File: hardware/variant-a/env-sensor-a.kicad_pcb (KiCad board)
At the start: 4 copper layers, 30 x 34 mm, 64 parts, among them J1 USB-C 16P, J2 Molex PicoBlade 3P, Q1 2N7002, SW1 SW_PROV, U1 ESP32-C6-MINI-1-N4, U2 SHT45-AD1F, U3 TPS62840DLC, U4 BQ24074RGTR, U5 USBLC6-2SC6

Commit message: build(sch): regenerate connector mounting-ground connectivity
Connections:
- J2 pad MP: unconnected-(J2-MountPin-PadMP) -> GND
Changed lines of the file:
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@@
 	(net 36 "unconnected-(J1-SBU1-PadA8)")
 	(net 37 "unconnected-(J1-SBU2-PadB8)")
-	(net 38 "unconnected-(J2-MountPin-PadMP)")
-	(net 39 "unconnected-(U1-IO0-Pad12)")
-	(net 40 "unconnected-(U1-IO15-Pad20)")
-	(net 41 "unconnected-(U1-IO4-Pad9)")
-	(net 42 "unconnected-(U1-IO5-Pad10)")
-	(net 43 "unconnected-(U1-NC-Pad21)")
-	(net 44 "unconnected-(U1-NC-Pad32)")
-	(net 45 "unconnected-(U1-NC-Pad33)")
-	(net 46 "unconnected-(U1-NC-Pad34)")
-	(net 47 "unconnected-(U1-NC-Pad35)")
-	(net 48 "unconnected-(U1-NC-Pad4)")
-	(net 49 "unconnected-(U1-NC-Pad7)")
-	(net 50 "unconnected-(U4-TMR-Pad14)")
+	(net 38 "unconnected-(U1-IO0-Pad12)")
+	(net 39 "unconnected-(U1-IO15-Pad20)")
+	(net 40 "unconnected-(U1-IO4-Pad9)")
+	(net 41 "unconnected-(U1-IO5-Pad10)")
+	(net 42 "unconnected-(U1-NC-Pad21)")
+	(net 43 "unconnected-(U1-NC-Pad32)")
+	(net 44 "unconnected-(U1-NC-Pad33)")
+	(net 45 "unconnected-(U1-NC-Pad34)")
+	(net 46 "unconnected-(U1-NC-Pad35)")
+	(net 47 "unconnected-(U1-NC-Pad4)")
+	(net 48 "unconnected-(U1-NC-Pad7)")
+	(net 49 "unconnected-(U4-TMR-Pad14)")
 	(footprint "sensorly:ESP32-C6-MINI-1"
 		(layer "F.Cu")
@@
 			(size 0.8 0.4)
 			(layers "F.Cu" "F.Mask" "F.Paste")
-			(net 48 "unconnected-(U1-NC-Pad4)")
+			(net 47 "unconnected-(U1-NC-Pad4)")
 		)
 		(pad "5" smd rect
@@
 			(size 0.8 0.4)
 			(layers "F.Cu" "F.Mask" "F.Paste")
-			(net 49 "unconnected-(U1-NC-Pad7)")
+			(net 48 "unconnected-(U1-NC-Pad7)")
 		)
 		(pad "8" smd rect
@@
 			(size 0.8 0.4)
 			(layers "F.Cu" "F.Mask" "F.Paste")
-			(net 41 "unconnected-(U1-IO4-Pad9)")
+			(net 40 "unconnected-(U1-IO4-Pad9)")
 		)
 		(pad "10" smd rect
@@
 			(size 0.8 0.4)
 			(layers "F.Cu" "F.Mask" "F.Paste")
-			(net 42 "unconnected-(U1-IO5-Pad10)")
+			(net 41 "unconnected-(U1-IO5-Pad10)")
 		)
 		(pad "11" smd rect
@@
 			(size 0.8 0.4)
 			(layers "F.Cu" "F.Mask" "F.Paste")
-			(net 39 "unconnected-(U1-IO0-Pad12)")
+			(net 38 "unconnected-(U1-IO0-Pad12)")
 		)
 		(pad "13" smd rect
@@
 			(size 0.8 0.4)
 			(layers "F.Cu" "F.Mask" "F.Paste")
-			(net 40 "unconnected-(U1-IO15-Pad20)")
+			(net 39 "unconnected-(U1-IO15-Pad20)")
 		)
 		(pad "21" smd rect
@@
 			(size 0.8 0.4)
 			(layers "F.Cu" "F.Mask" "F.Paste")
-			(net 43 "unconnected-(U1-NC-Pad21)")
+			(net 42 "unconnected-(U1-NC-Pad21)")
 		)
 		(pad "22" smd rect
@@
 			(size 0.8 0.4)
 			(layers "F.Cu" "F.Mask" "F.Paste")
-			(net 44 "unconnected-(U1-NC-Pad32)")
+			(net 43 "unconnected-(U1-NC-Pad32)")
 		)
 		(pad "33" smd rect
@@
 			(size 0.8 0.4)
 			(layers "F.Cu" "F.Mask" "F.Paste")
-			(net 45 "unconnected-(U1-NC-Pad33)")
+			(net 44 "unconnected-(U1-NC-Pad33)")
 		)
 		(pad "34" smd rect
@@
 			(size 0.8 0.4)
 			(layers "F.Cu" "F.Mask" "F.Paste")
-			(net 46 "unconnected-(U1-NC-Pad34)")
+			(net 45 "unconnected-(U1-NC-Pad34)")
 		)
 		(pad "35" smd rect
@@
 			(size 0.8 0.4)
 			(layers "F.Cu" "F.Mask" "F.Paste")
-			(net 47 "unconnected-(U1-NC-Pad35)")
+			(net 46 "unconnected-(U1-NC-Pad35)")
 		)
 		(pad "36" smd rect
@@
 		(pad "MP" smd roundrect (at -3.8 0.5 90.0) (size 2.1 3)
 			(layers "F.Cu" "F.Mask" "F.Paste") (roundrect_rratio 0.119048)
-			(net 38 "unconnected-(J2-MountPin-PadMP)")
+			(net 12 "GND")
 		)
 		(pad "MP" smd roundrect (at 3.8 0.5 90.0) (size 2.1 3)
 			(layers "F.Cu" "F.Mask" "F.Paste") (roundrect_rratio 0.119048)
-			(net 38 "unconnected-(J2-MountPin-PadMP)")
+			(net 12 "GND")
 		)
 		(embedded_fonts no)
@@
 			(layers "F.Cu" "F.Mask" "F.Paste")
 			(roundrect_rratio 0.2)
-			(net 50 "unconnected-(U4-TMR-Pad14)")
+			(net 49 "unconnected-(U4-TMR-Pad14)")
 		)
 		(pad "15" smd roundrect

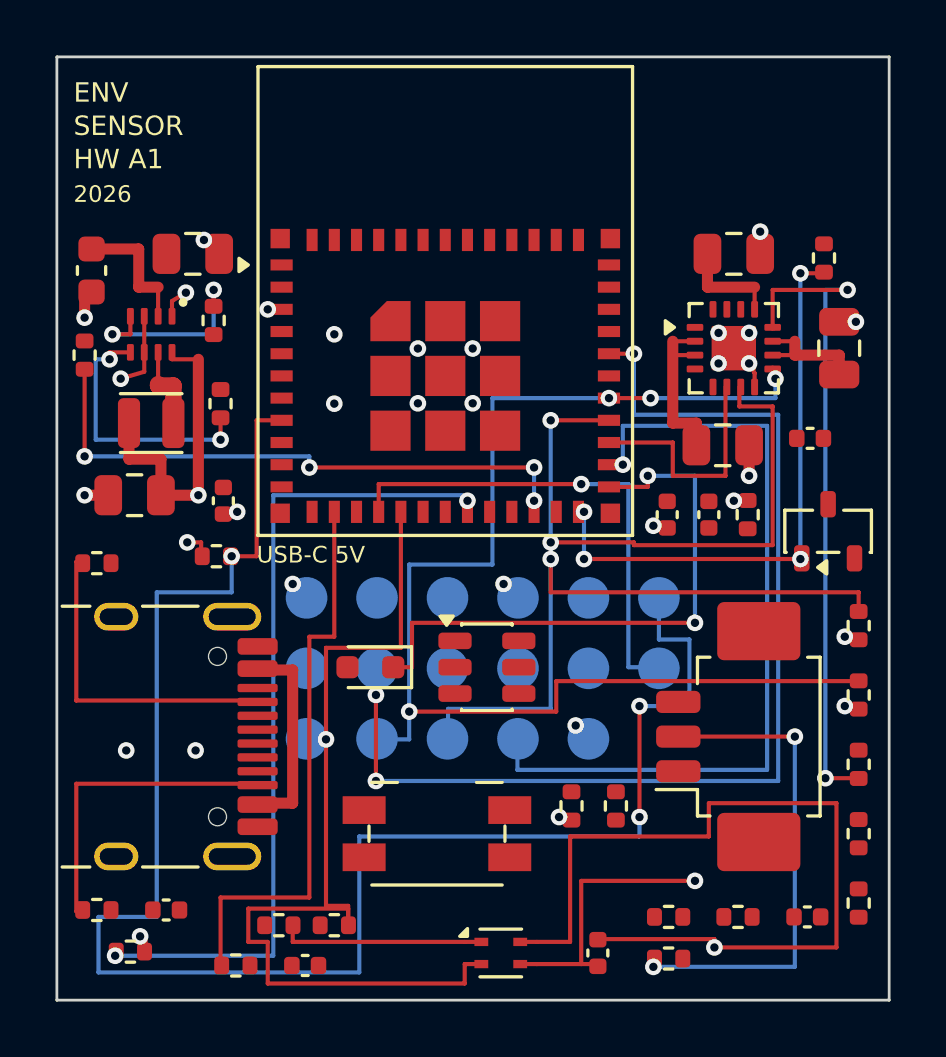
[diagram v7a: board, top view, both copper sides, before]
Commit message: build(boardgen): regenerate paste-safe routing for both variants
Regenerate from the ordinary-via paste separation correction. Fresh KiCad reports show zero errors, warnings and parity differences; record the exact incomplete development counts of A42/B34. Fabrication still requires complete routing and accepted qualification evidence.
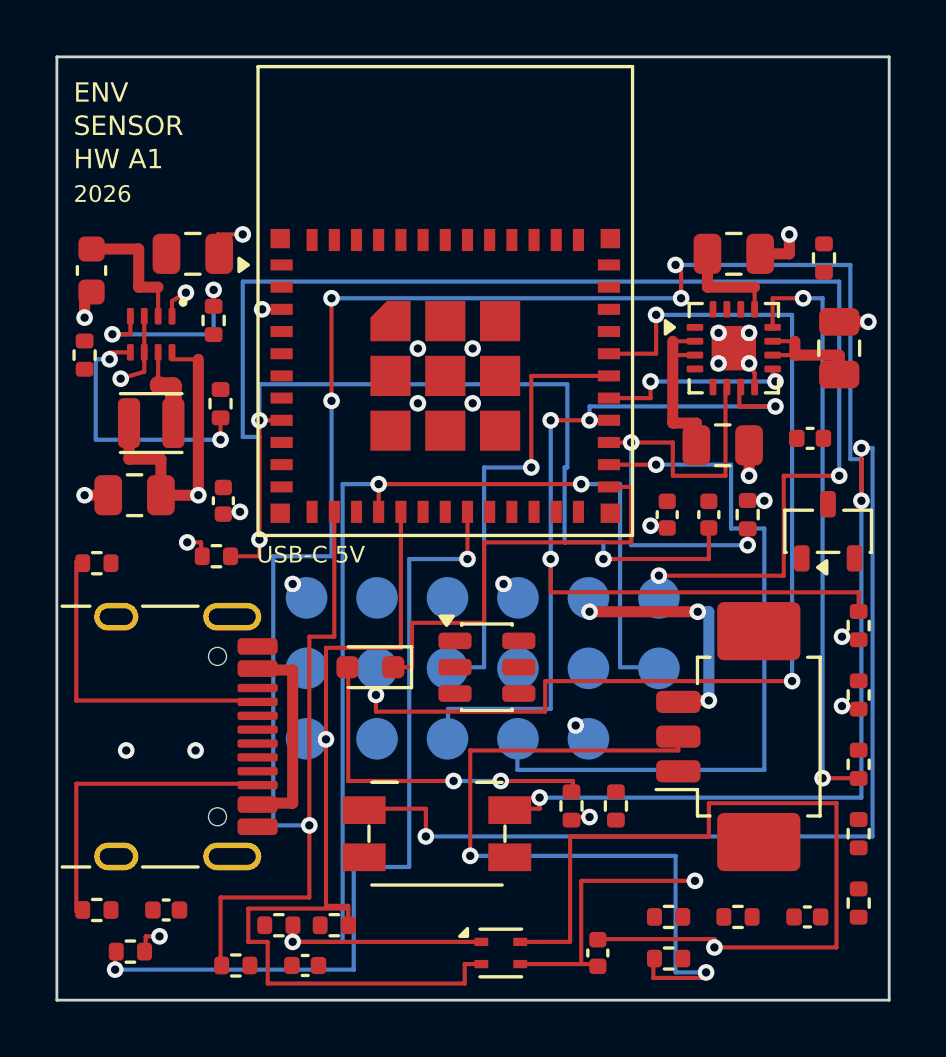
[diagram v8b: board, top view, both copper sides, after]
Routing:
- net BTN_PROV: track 20.5 -> 131.5 mm, vias 0 -> 9
- net CHG_N: track 45.2 -> 7.20 mm, vias 4 -> 2
- net BOOT_MODE_H: track 21.3 -> 0.00 mm, vias 4 -> 0
- net CHARGE_ENABLE: track 20.6 -> 0.00 mm, vias 4 -> 0
- net SDA: track 25.1 -> 45.3 mm, vias 1 -> 3
- net EN: track 62.4 -> 81.1 mm, vias 3 -> 5
- net UART_RX: track 0.00 -> 16.3 mm, vias 0 -> 1
- net LED_A: track 0.00 -> 12.6 mm, vias 0 -> 2
- net PACK_TS: track 17.9 -> 27.3 mm
- net VBAT: track 6.20 -> 15.3 mm, vias 0 -> 3
- net USB_ISEL: track 8.60 -> 17.1 mm, vias 0 -> 2
- net PG_N: track 45.3 -> 39.5 mm, vias 3 -> 4
- net LED_N: track 21.3 -> 15.9 mm, vias 2 -> 0
- net TEST_MODE: track 29.6 -> 26.6 mm
- net ILIM: track 23.7 -> 21.5 mm
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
